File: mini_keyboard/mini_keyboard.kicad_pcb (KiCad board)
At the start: 2 copper layers, 158.8 x 114.3 mm, 37 parts, among them U1 MX1A-11NN, U10 MX1A-11NN, U100 DEV-15583, U11 MX1A-11NN, U12 MX1A-11NN, U13 MX1A-11NN, U14 MX1A-11NN, U15 MX1A-11NN, U16 MX1A-11NN, U17 MX1A-11NN, U18 MX1A-11NN, U19 MX1A-11NN, U20 MX1A-11NN, U21 MX1A-11NN, U22 MX1A-11NN, U23 MX1A-11NN, U24 MX1A-11NN, U25 MX1A-11NN, U26 MX1A-11NN, U27 MX1A-11NN, U29 MX1A-11NN, U3 MX1A-11NN, U30 MX1A-11NN, U31 MX1A-11NN, U32 MX1A-11NN, U33 MX1A-11NN, U34 MX1A-11NN, U36 MX1A-11NN, U37 MX1A-11NN, U38 MX1A-11NN, U39 MX1A-11NN, U4 MX1A-11NN, U5 MX1A-11NN, U6 MX1A-11NN, U7 MX1A-11NN, U8 MX1A-11NN, U9 MX1A-11NN

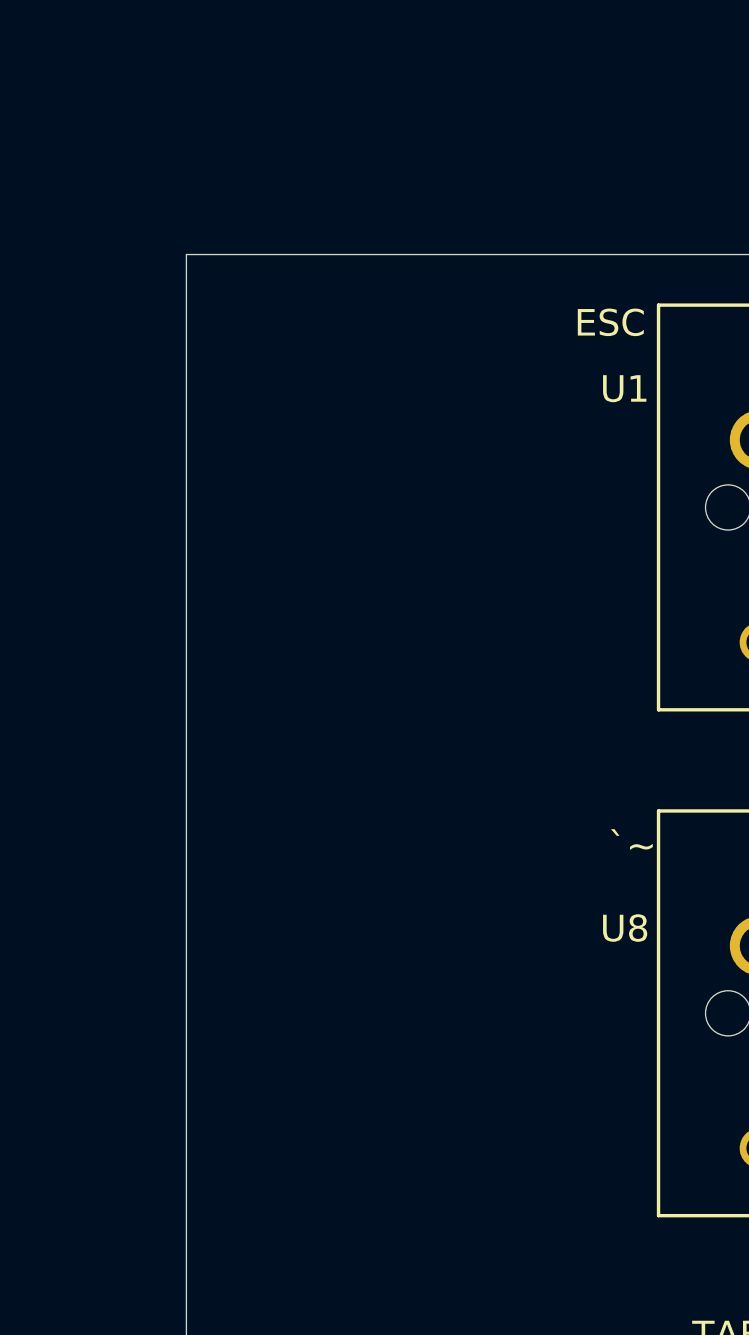
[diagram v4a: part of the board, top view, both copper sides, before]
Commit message: Looking at Arduino 33 IOT for CPU to get arduino-cli support
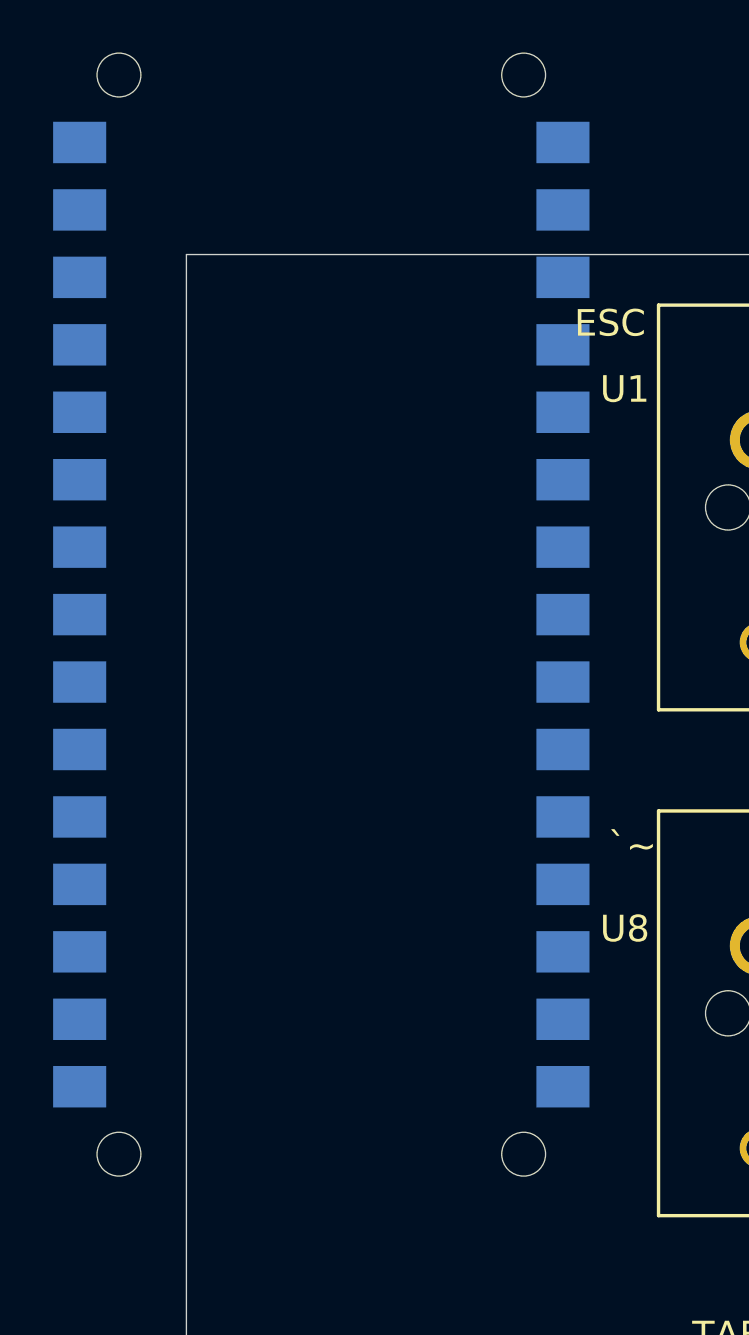
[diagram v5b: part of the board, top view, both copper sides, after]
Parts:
- added U101: ABX00027, pedrolib:MODULE_ABX00027, B.Cu at (30.5, 39.4)

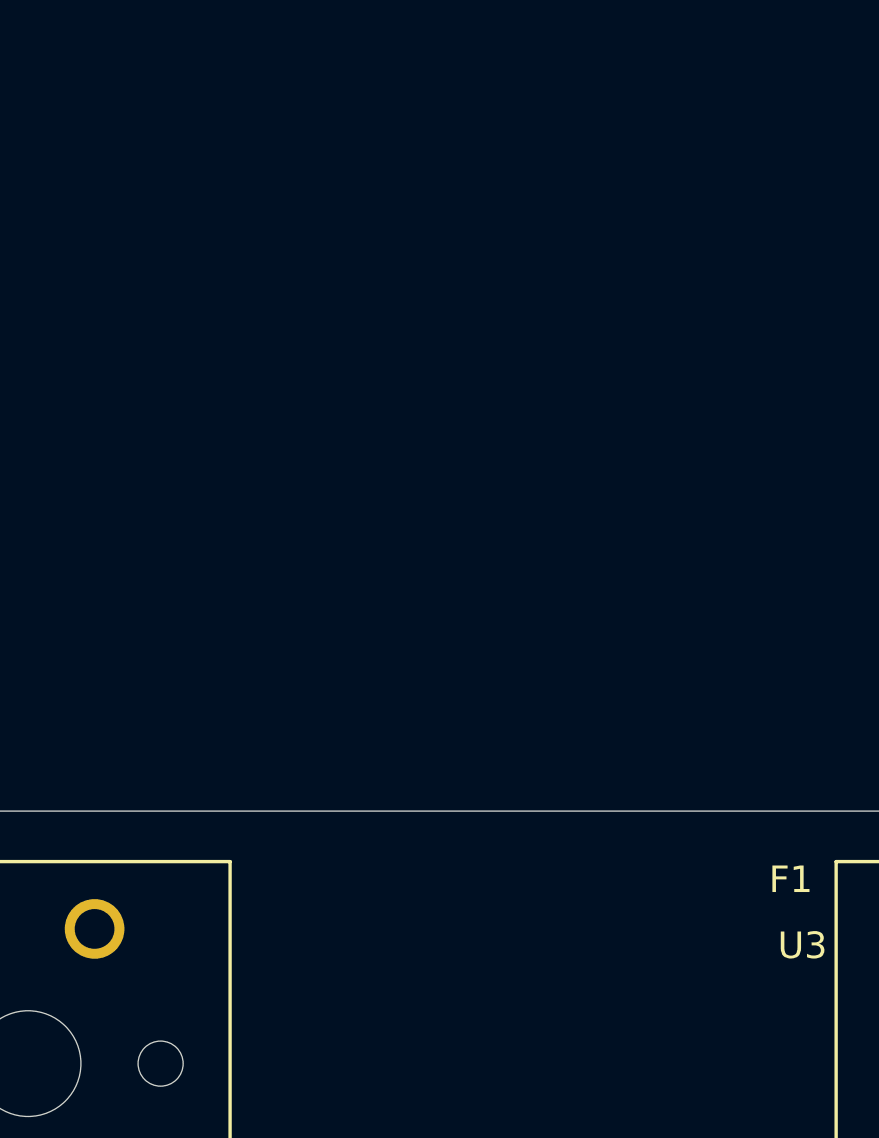
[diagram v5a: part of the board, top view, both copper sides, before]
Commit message: prepping to wire the switches and diodes to the array
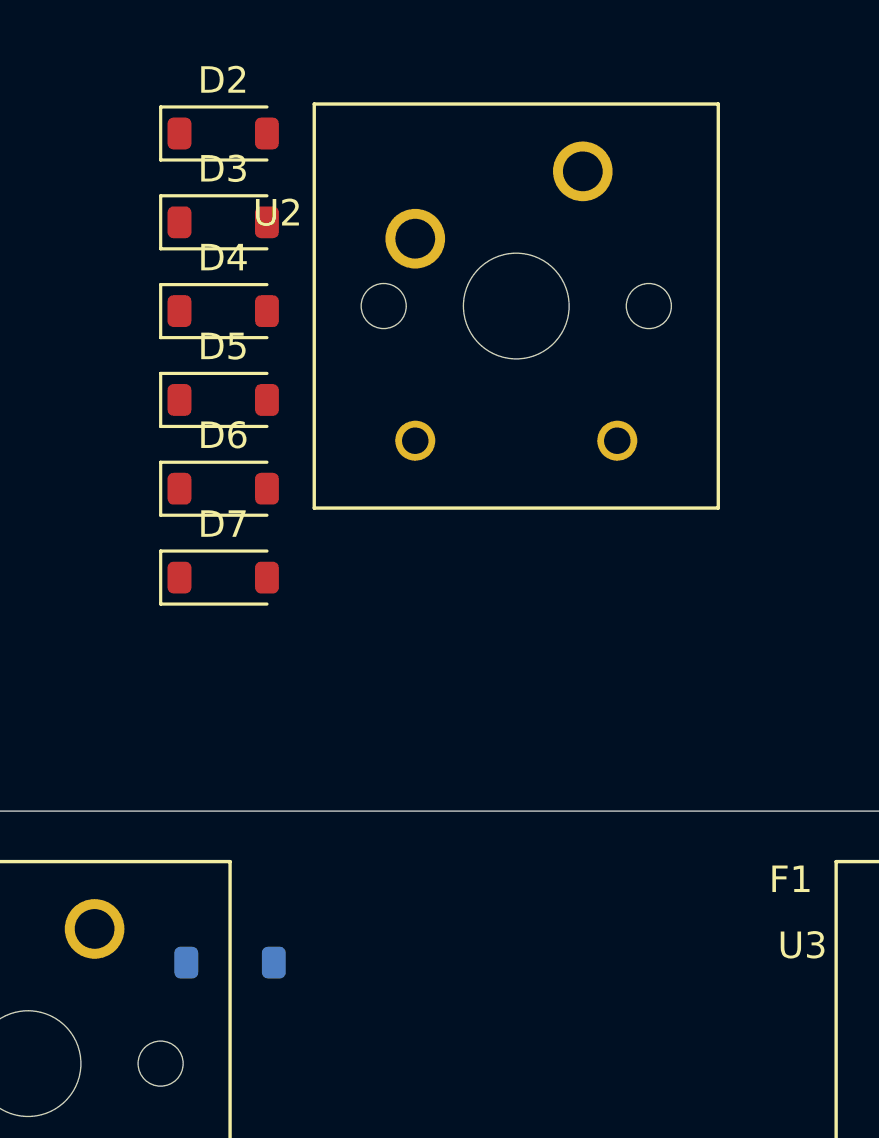
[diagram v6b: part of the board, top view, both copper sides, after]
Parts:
- added D1: 1N4148W, Diode_SMD:D_SOD-123, B.Cu at (58.4, 31.1)
- added D2: 1N4148W, Diode_SMD:D_SOD-123, F.Cu at (58.2, -0.16)
- added D3: 1N4148W, Diode_SMD:D_SOD-123, F.Cu at (58.2, 3.19)
- added D4: 1N4148W, Diode_SMD:D_SOD-123, F.Cu at (58.2, 6.54)
- added D5: 1N4148W, Diode_SMD:D_SOD-123, F.Cu at (58.2, 9.89)
- added D6: 1N4148W, Diode_SMD:D_SOD-123, F.Cu at (58.2, 13.2)
- added D7: 1N4148W, Diode_SMD:D_SOD-123, F.Cu at (58.2, 16.6)
- added U2: MX1A-11NN, pedrolib:CHERRY_MX1A-11NN_SWITCH, F.Cu at (69.2, 6.35)
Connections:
- U1 pad P$1: unconnected-(U1-PadP$1) -> Net-(D1-A)
